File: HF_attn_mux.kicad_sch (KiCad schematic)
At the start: 29 parts, among them IC10 PE4250MLI-Z, IC11 PE4250MLI-Z, IC12 PE4250MLI-Z, IC13 PE4250MLI-Z, J12 SMA, J29 Conn_01x04, J30 Conn_01x06, U14 PHA-13LN, U15 PAT1220-C-6DB, U16 PAT1220-C-6DB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

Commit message: First finished draft
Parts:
- IC10, IC11, IC12, IC13: footprint SOP65P488X107-8N -> SamacSys_Parts:SOP65P488X107-8N
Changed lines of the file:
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@@
     (property "Reference" "IC10" (id 0) (at 146.05 19.05 0))
     (property "Value" "PE4250MLI-Z" (id 1) (at 146.05 21.59 0))
-    (property "Footprint" "SOP65P488X107-8N" (id 2) (at 161.29 24.13 0)
+    (property "Footprint" "SamacSys_Parts:SOP65P488X107-8N" (id 2) (at 161.29 24.13 0)
       (effects (font (size 1.27 1.27)) (justify left) hide)
     )
@@
     (property "Reference" "IC11" (id 0) (at 234.95 41.91 0))
     (property "Value" "PE4250MLI-Z" (id 1) (at 234.95 39.37 0))
-    (property "Footprint" "SOP65P488X107-8N" (id 2) (at 219.71 36.83 0)
+    (property "Footprint" "SamacSys_Parts:SOP65P488X107-8N" (id 2) (at 219.71 36.83 0)
       (effects (font (size 1.27 1.27)) (justify left) hide)
     )
@@
     (property "Reference" "IC12" (id 0) (at 128.27 60.96 0))
     (property "Value" "PE4250MLI-Z" (id 1) (at 128.27 63.5 0))
-    (property "Footprint" "SOP65P488X107-8N" (id 2) (at 143.51 66.04 0)
+    (property "Footprint" "SamacSys_Parts:SOP65P488X107-8N" (id 2) (at 143.51 66.04 0)
       (effects (font (size 1.27 1.27)) (justify left) hide)
     )
@@
     (property "Reference" "IC13" (id 0) (at 243.84 83.82 0))
     (property "Value" "PE4250MLI-Z" (id 1) (at 243.84 81.28 0))
-    (property "Footprint" "SOP65P488X107-8N" (id 2) (at 228.6 78.74 0)
-      (effects (font (size 1.27 1.27)) (justify left) hide)
-    )
+    (property "Footprint" "SamacSys_Parts:SOP65P488X107-8N" (id 2) (at 228.6 78.74 0)
+      (effects (font (size 1.27 1.27)) (justify left) hide)
+    )

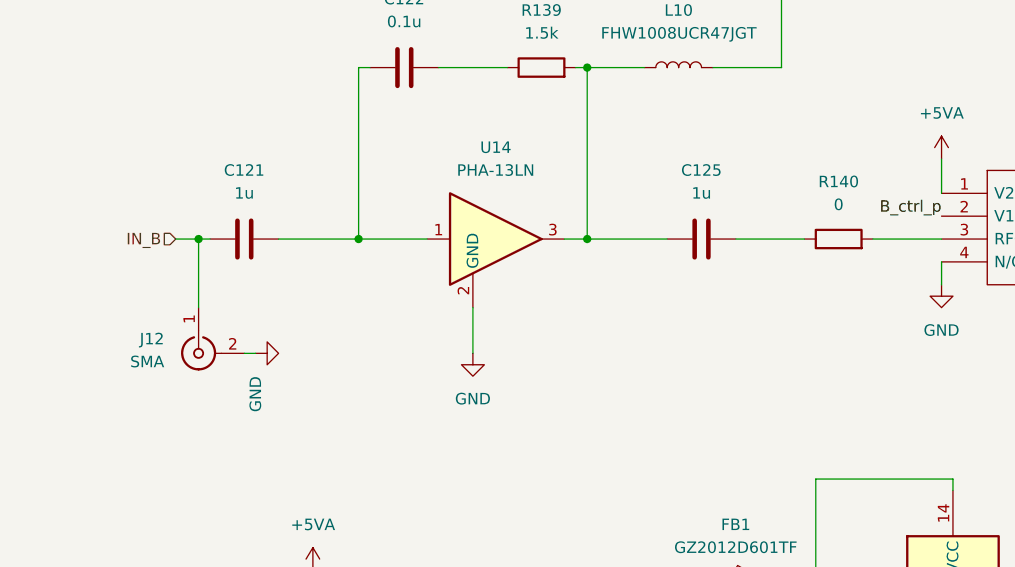
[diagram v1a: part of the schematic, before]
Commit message: Version 1.0 submitted to JLCPCB
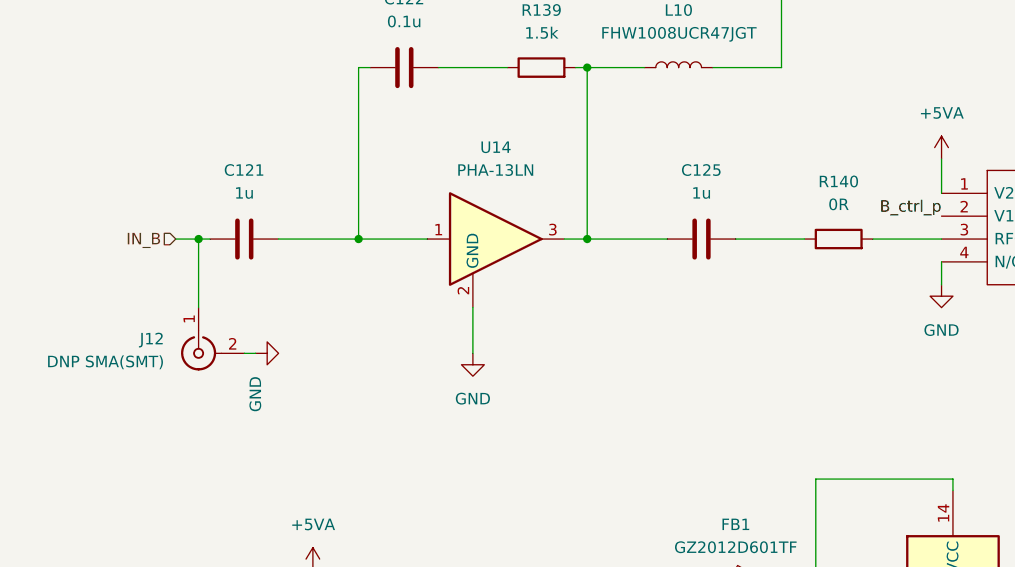
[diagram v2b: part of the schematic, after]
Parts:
- J12: value SMA -> DNP SMA(SMT)
- R140: value 0 -> 0R
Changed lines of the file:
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@@
       (effects (font (size 1.27 1.27)) (justify left))
     )
-    (property "Value" "SMA" (id 1) (at 22.86 87.3124 90)
+    (property "Value" "DNP SMA(SMT)" (id 1) (at 22.86 87.3124 90)
       (effects (font (size 1.27 1.27)) (justify left))
     )
@@
     (in_bom yes) (on_board yes) (fields_autoplaced)
     (property "Reference" "R140" (id 0) (at 97.79 67.31 90))
-    (property "Value" "0" (id 1) (at 97.79 69.85 90))
+    (property "Value" "0R" (id 1) (at 97.79 69.85 90))
     (property "Footprint" "Resistor_SMD:R_0805_2012Metric" (id 2) (at 97.79 75.438 90)
       (effects (font (size 1.27 1.27)) hide)
